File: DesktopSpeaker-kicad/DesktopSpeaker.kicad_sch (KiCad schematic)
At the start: 10 parts, among them J1 USB_C_Receptacle_USB2.0_16P, J2 HEAD_OUT, J3 AUX_IN, U1 BM83SM1-00TA, U10 TPA6132A2RTER, U6 TAS5825MRHBR, U7 TAS5825MRHBR, U8 TS5A23157DGSR, U9 TS5A23157DGSR

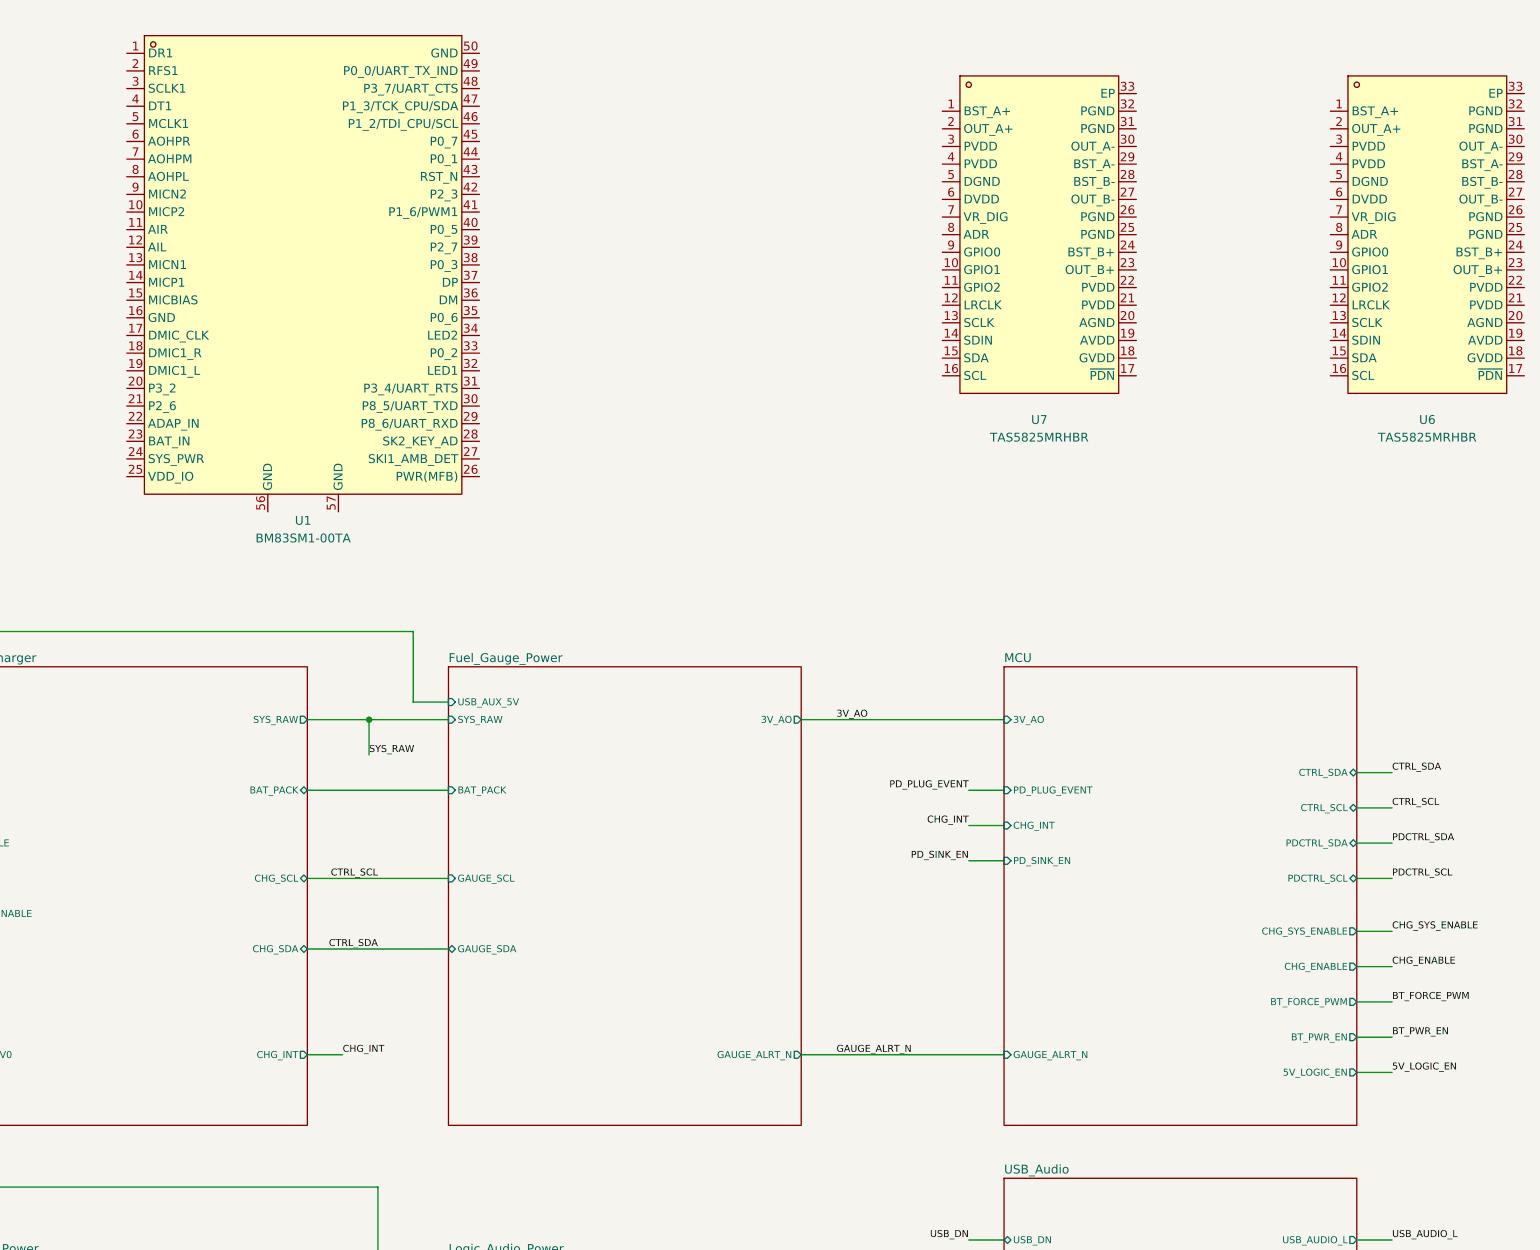
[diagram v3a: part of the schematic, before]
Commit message: Capture Bluetooth BM83 child sheet with MCU UART/reset/MFB connections
Co-Authored-By: Claude Sonnet 5.5 <noreply@anthropic.com>
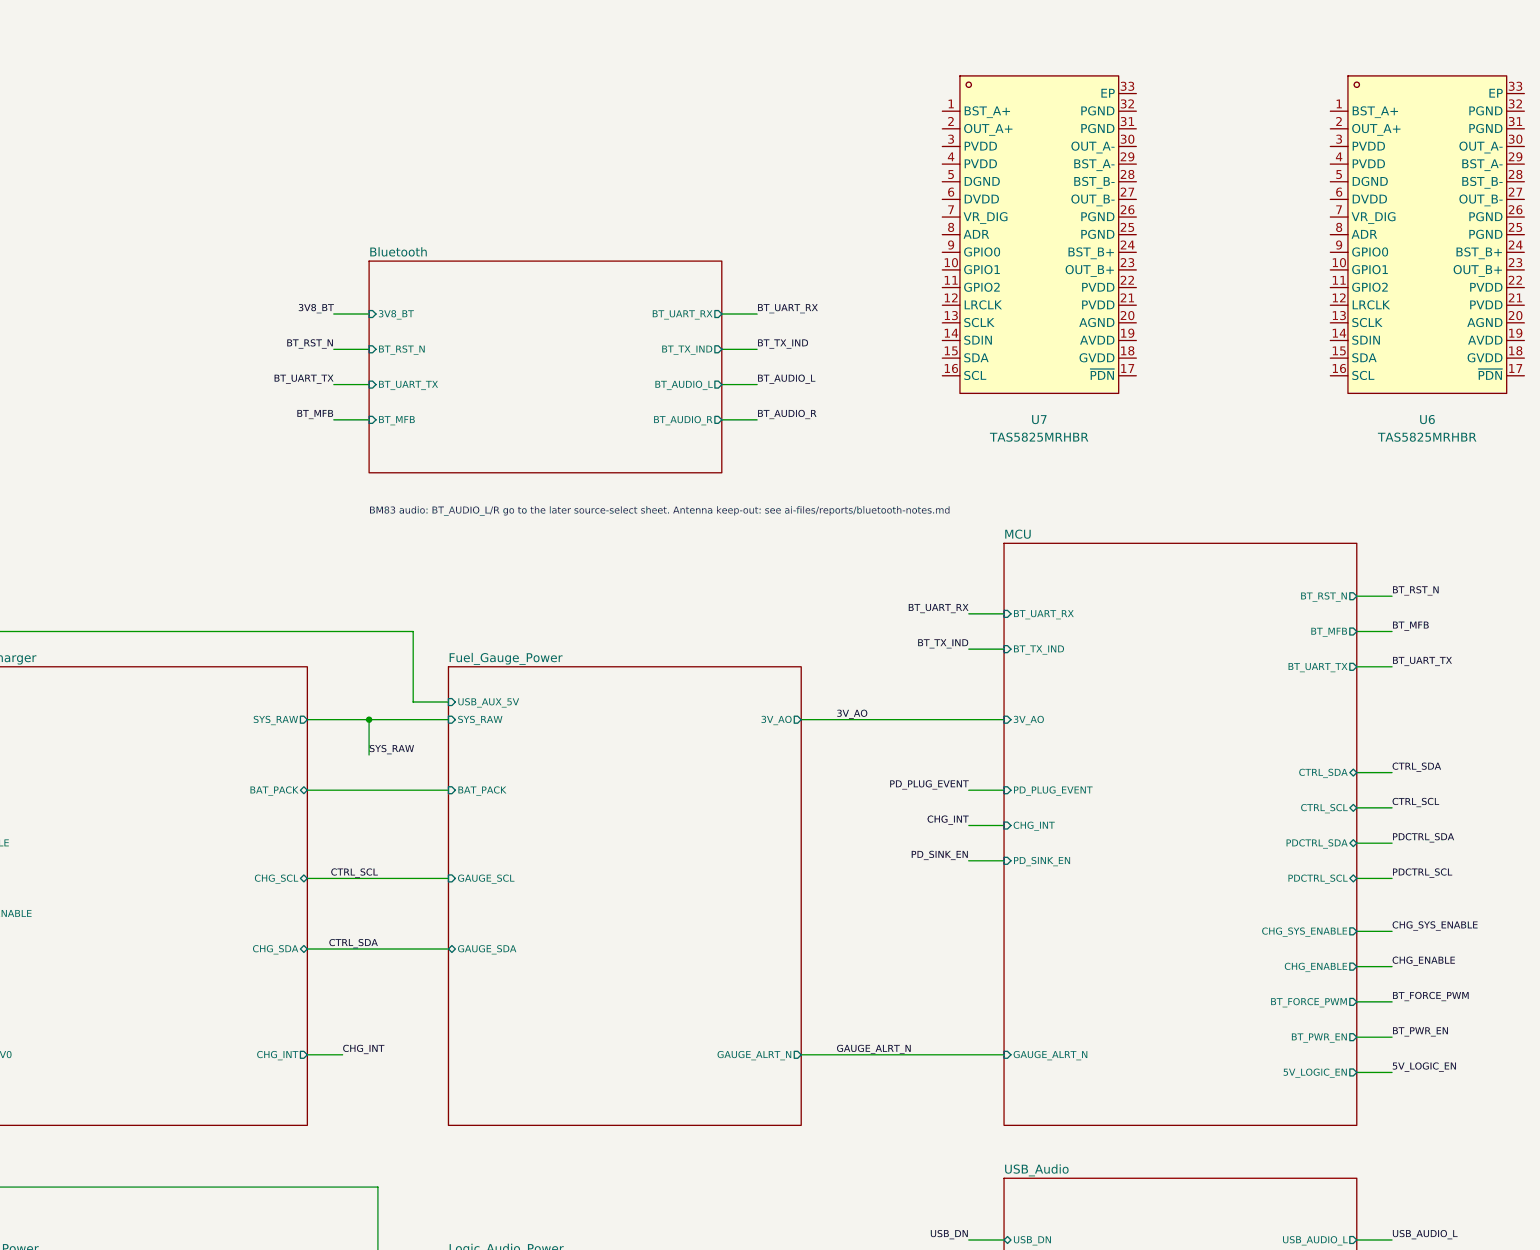
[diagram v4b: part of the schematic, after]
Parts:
- removed U1: BM83SM1-00TA, DesktopSpeaker:BM83SM1-00TA, symbol BM83SM1-00TA:BM83SM1-00TA
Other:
- added sheet Bluetooth (Bluetooth.kicad_sch)
- sheet MCU ports: added BT_MFB, BT_RST_N, BT_TX_IND, BT_UART_RX, BT_UART_TX; removed none
- note added: "BM83 audio: BT_AUDIO_L/R go to the later source-select sheet. Antenna keep-out: see ai-files/reports/bluetooth-notes.md"

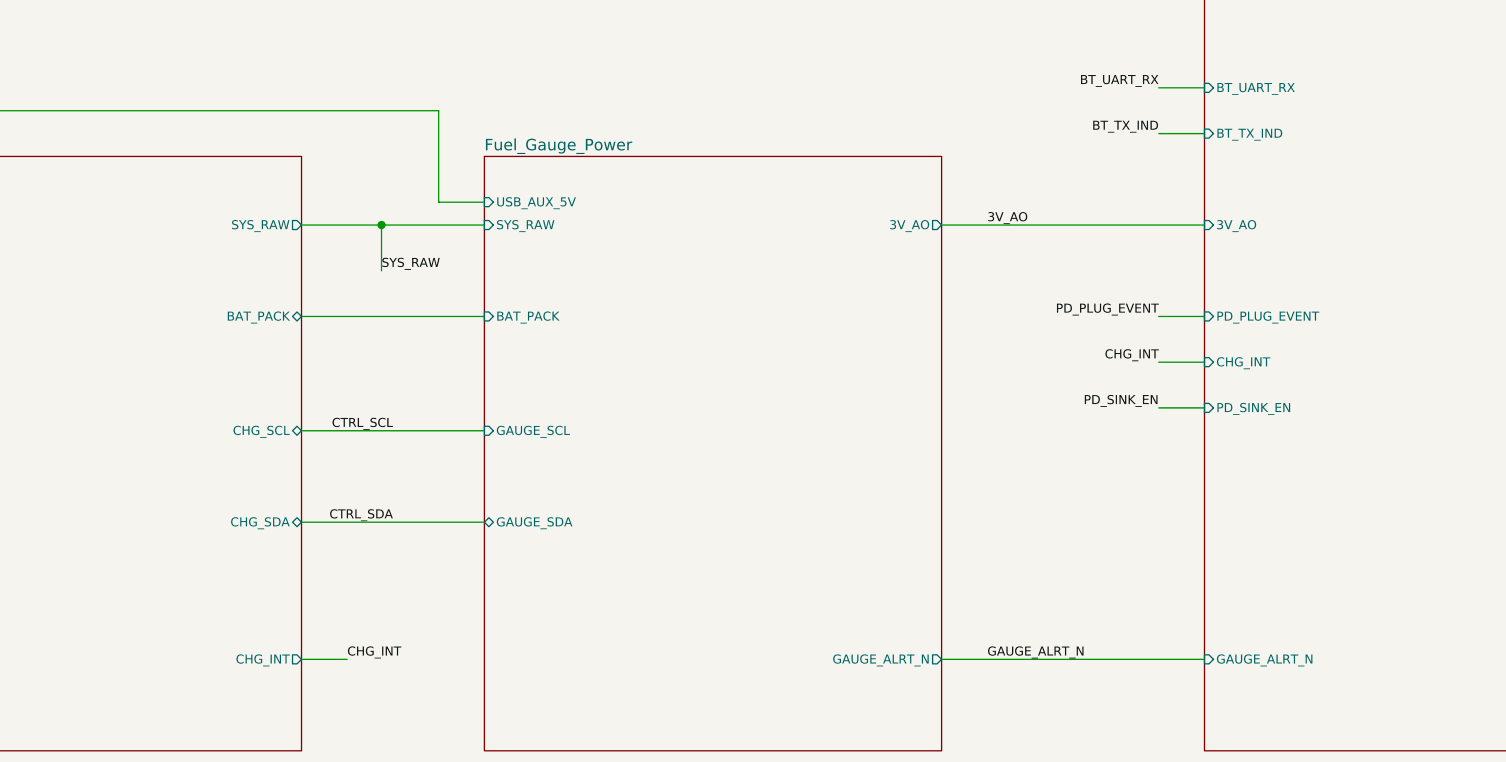
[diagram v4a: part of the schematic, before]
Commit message: Swap MCU to STM32G071RBT6; full audio-chain pin allocation and QON sense
Co-Authored-By: Claude Sonnet 5.5 <noreply@anthropic.com>
Claude-Session: https://claude.ai/code/session_01N5RHheWSjDFDPbKVD5YVeJ
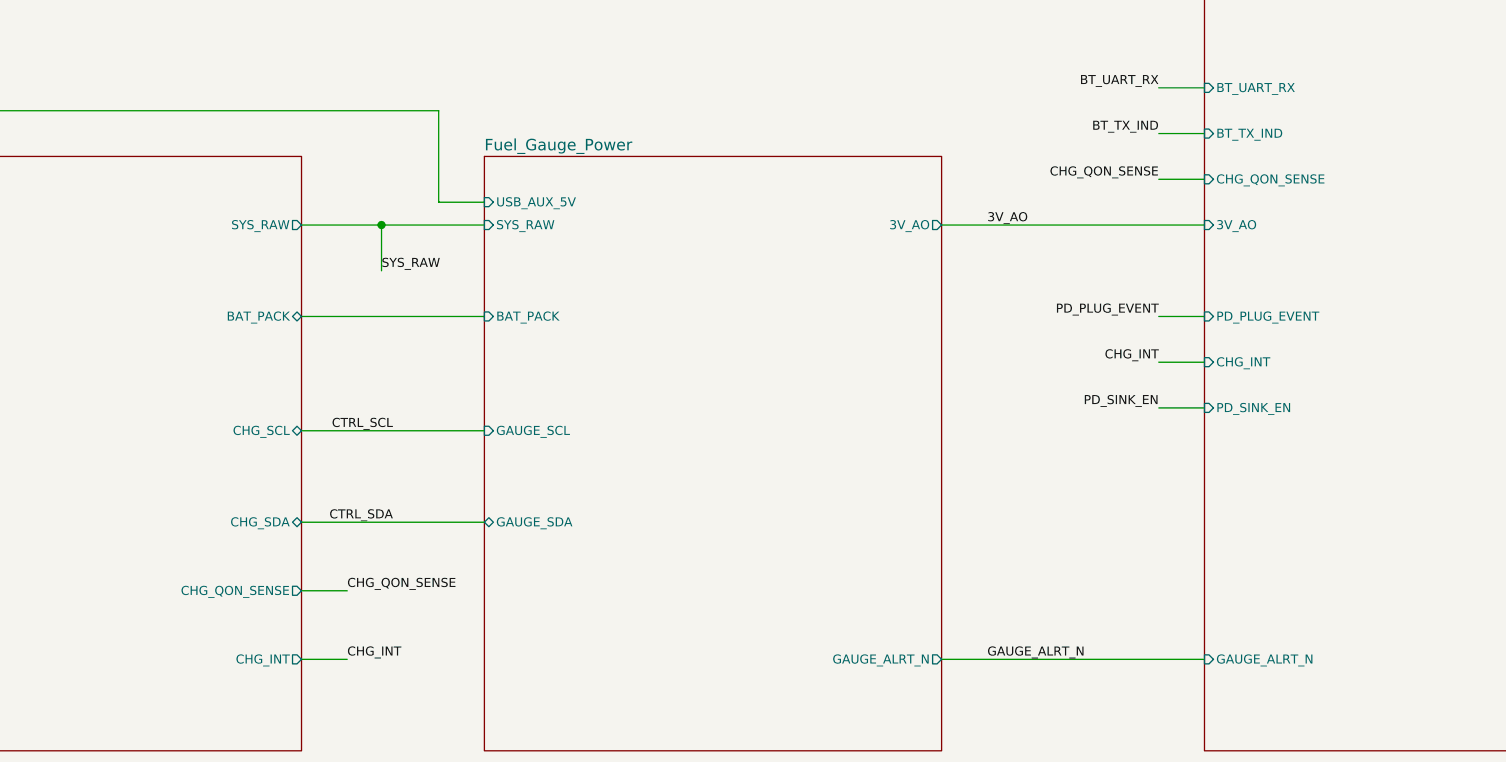
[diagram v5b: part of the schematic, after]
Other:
- sheet Battery_Charger ports: added CHG_QON_SENSE; removed none
- sheet MCU ports: added CHG_QON_SENSE; removed none

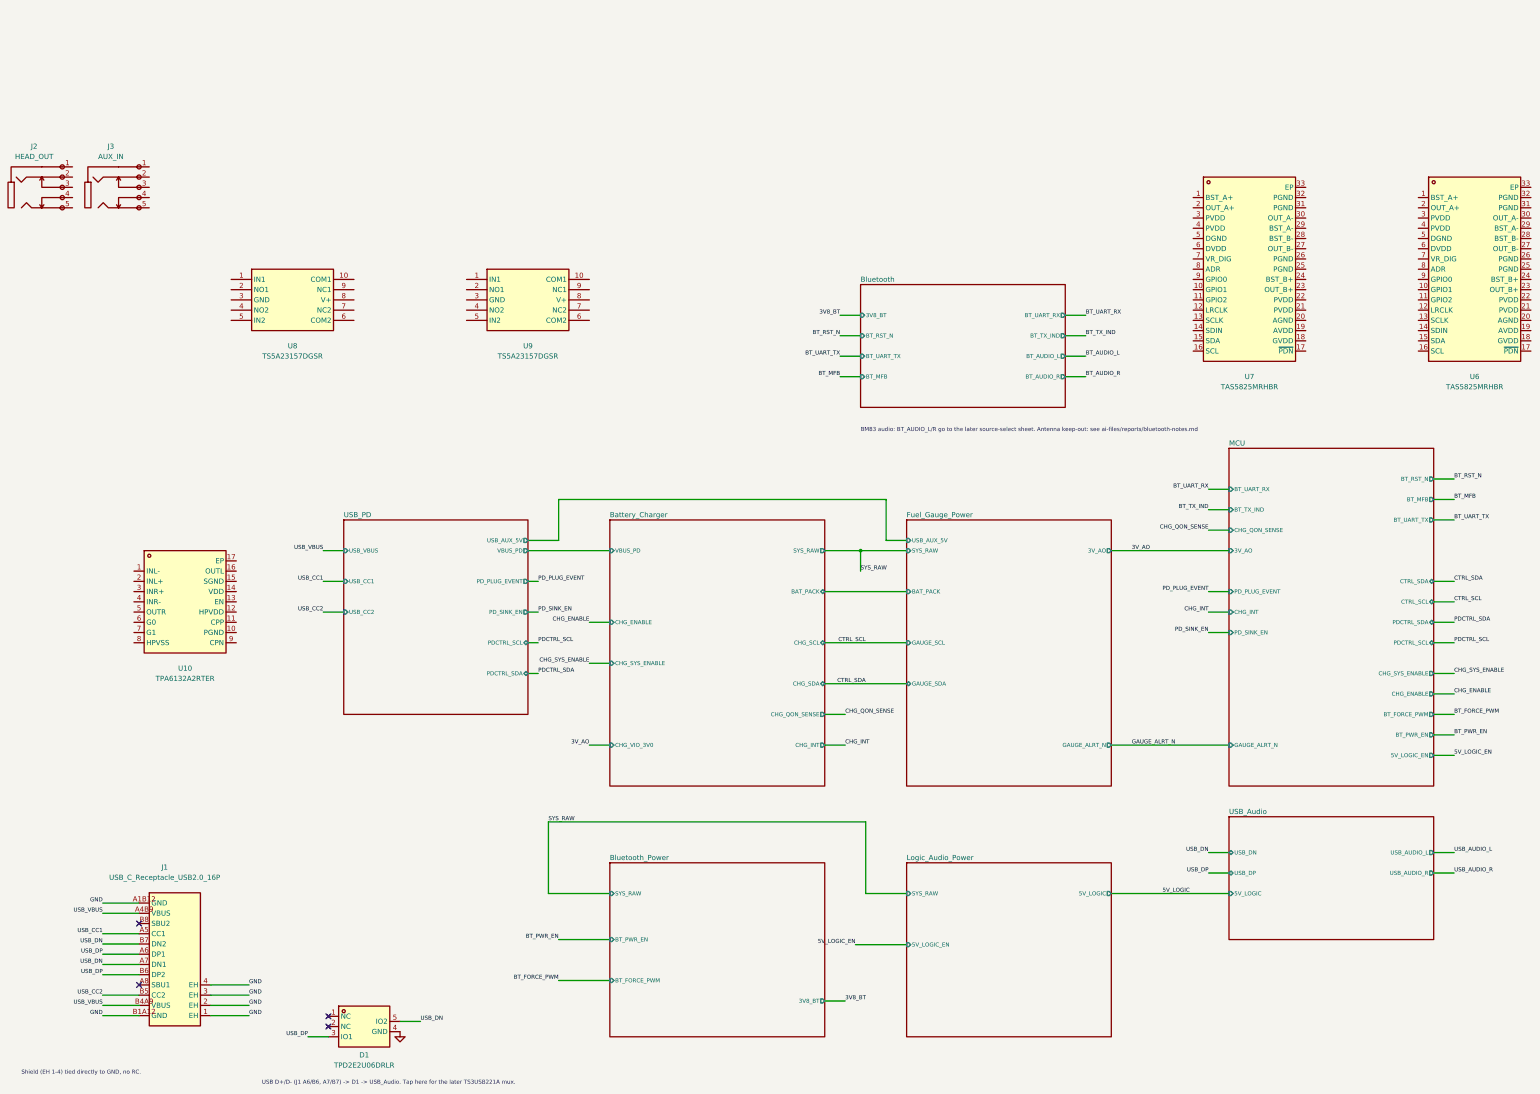
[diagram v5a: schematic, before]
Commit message: Capture Source_Select_ADC sheet (PCM1862, 3V3_AUDIO LDO, codec load switch)
Co-Authored-By: Claude Sonnet 5.5 <noreply@anthropic.com>
Claude-Session: https://claude.ai/code/session_01N5RHheWSjDFDPbKVD5YVeJ
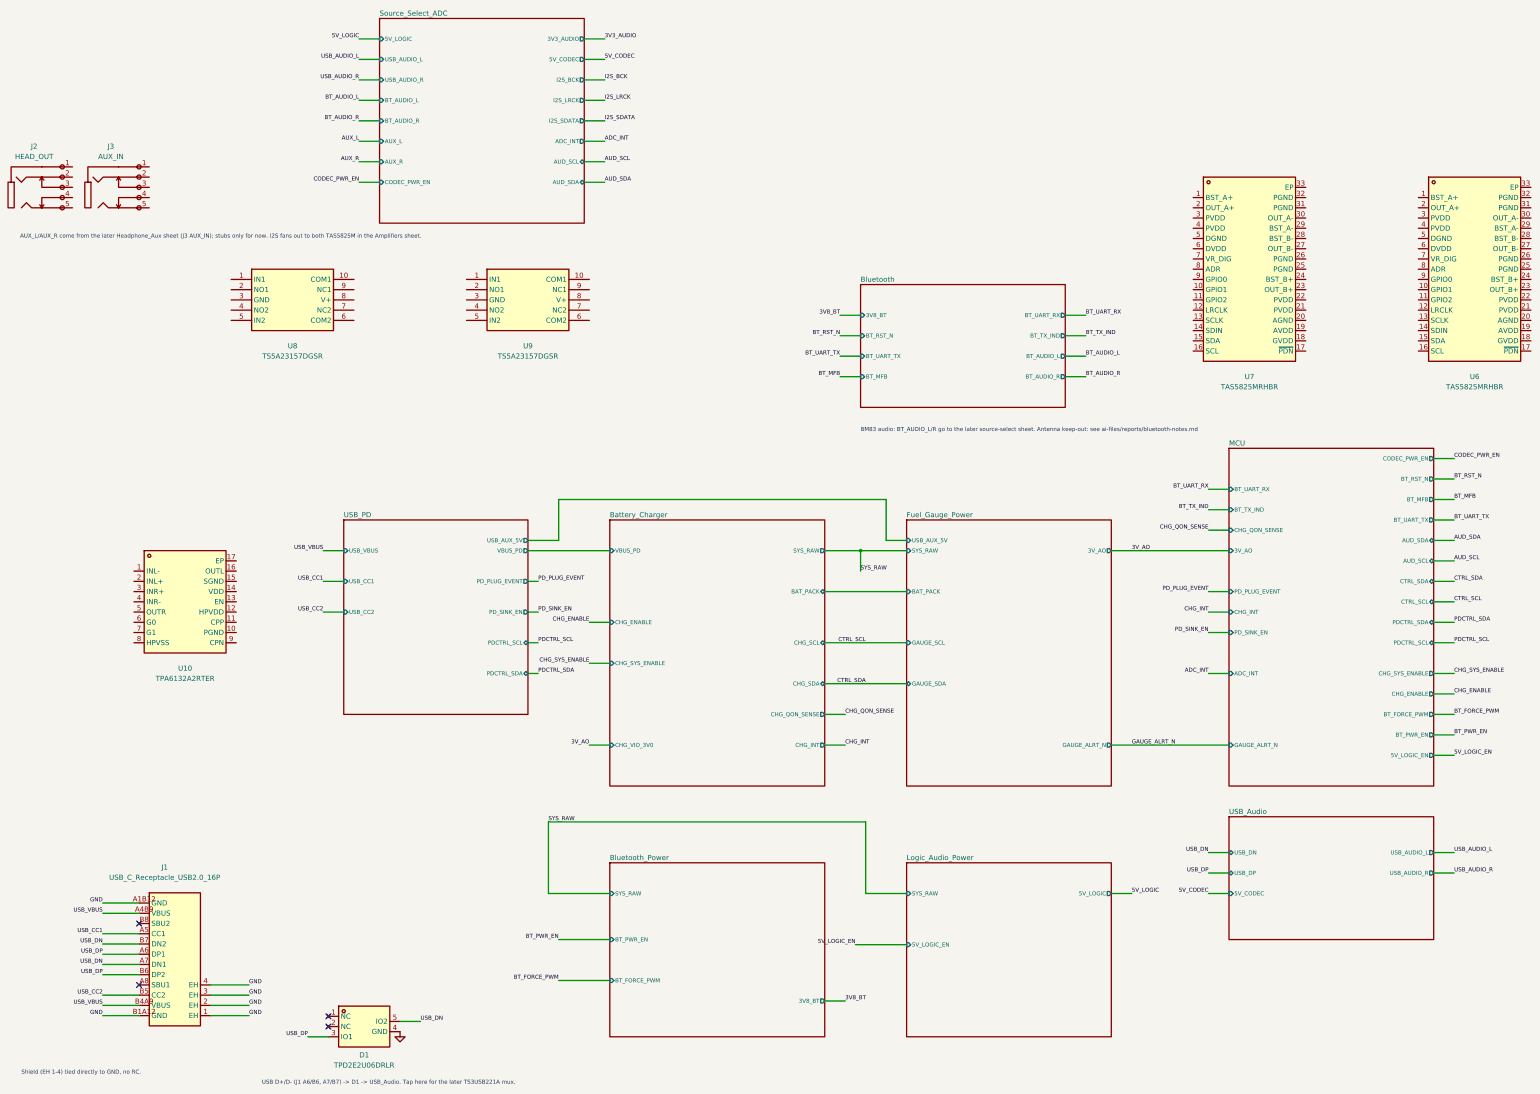
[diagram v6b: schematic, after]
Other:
- added sheet Source_Select_ADC (Source_Select_ADC.kicad_sch)
- sheet MCU ports: added ADC_INT, AUD_SCL, AUD_SDA, CODEC_PWR_EN; removed none
- sheet USB_Audio ports: added 5V_CODEC; removed 5V_LOGIC
- note added: "AUX_L/AUX_R come from the later Headphone_Aux sheet (J3 AUX_IN); stubs only for now. I2S fans out to both TAS5825M in the Amplifiers sheet."
